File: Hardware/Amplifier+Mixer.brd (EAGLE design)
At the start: 140 x 140 mm, 192 parts, among them IC1 7812, IC2 7805, IC3 7912, IC4 OPA134PA, IC5 OPA134PA, IC6 MEGA8-AI, IC7 74HCT04, IC8 LM358D, IC9 LM358D, J1 6MM, J10 JST-XH2, J2 6MM, J3 6MM, J4 6MM, J5 TERMINAL-BLOCK-2PLUG-IN, J6 TERMINAL-BLOCK-2PLUG-IN, J7 ENCODER, J8 DISPLAY, J9 USB, K1 12V 8A, K2 12V 8A, T1 BC817, T2 BC817, T3 BC817, T4 BC817, U1 LM1117-3.3, U2 10k, U3 10k, U4 10k, U5 10k, U6 TDA7498L, U7 10k, U8 10k, X1 RCA-4-CHANNEL, X2 JST-XH2, X3 ICSP

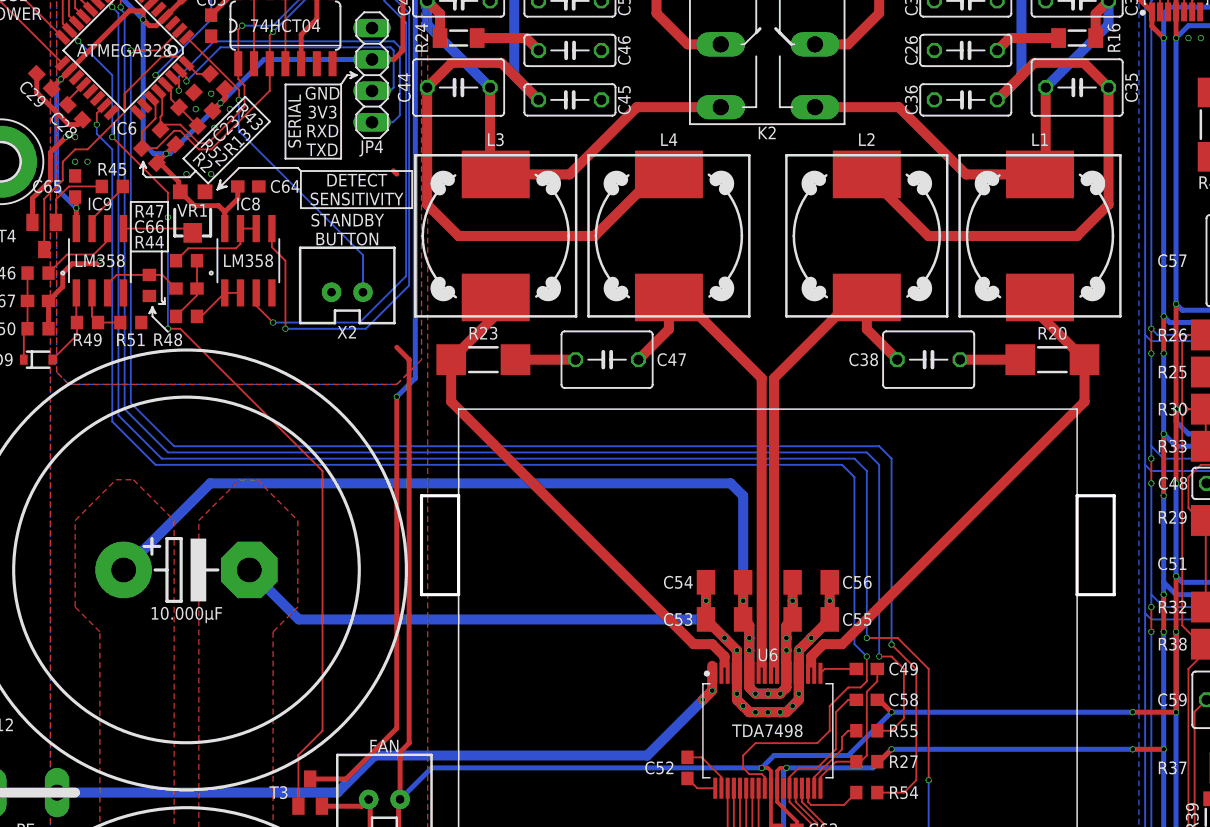
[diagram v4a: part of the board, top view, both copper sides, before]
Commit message: added temp sensor for amp chip heatsink
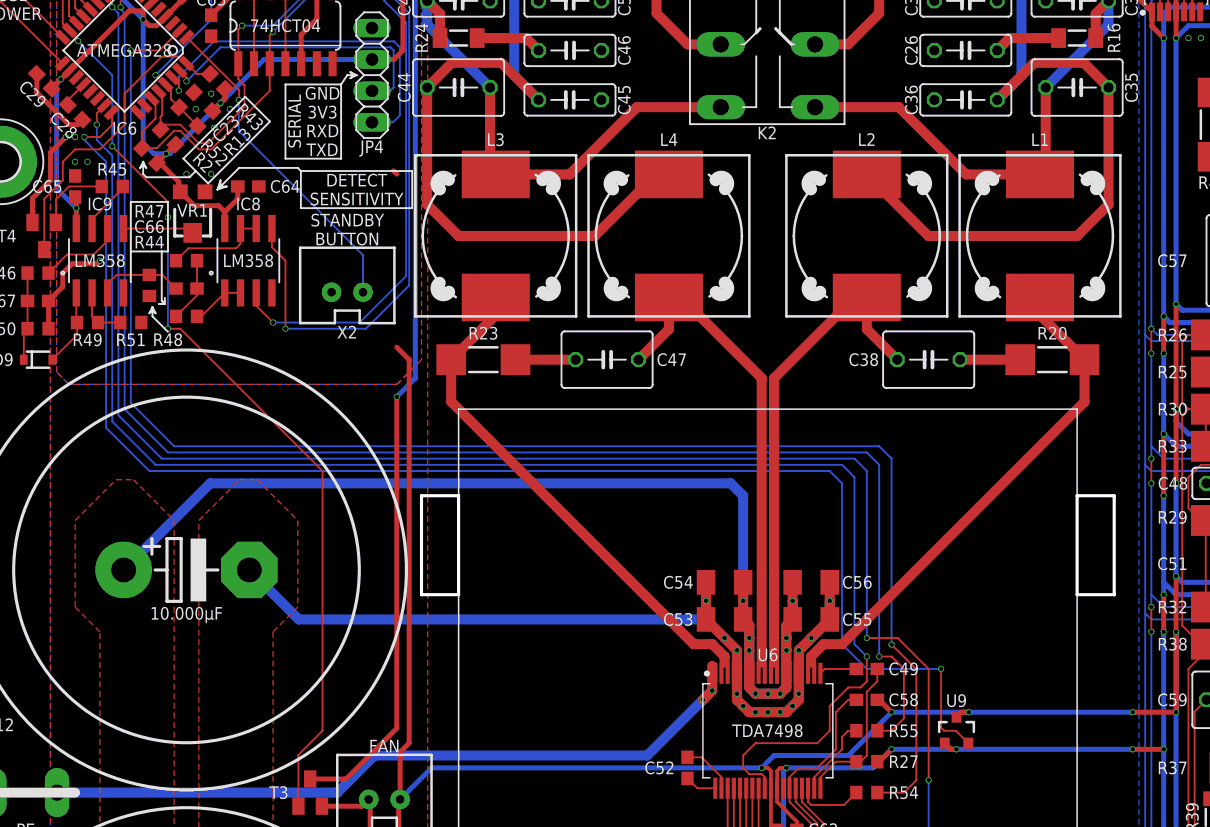
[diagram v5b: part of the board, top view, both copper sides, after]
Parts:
- added U9: MCP9700SMD, SparkFun-Sensors:SOT23-3
- renumbered U$1 to KK3
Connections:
- new net T_SENSE: IC6.24, U9.2
- net +3V3: now also U9.1
- net DGND: now also U9.3
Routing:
- net T_SENSE: track 0.00 -> 118.6 mm, vias 0 -> 2
- net DGND: track 407.7 -> 408.8 mm, vias 36 -> 37
- net +3V3: track 492.7 -> 493.8 mm, vias 26 -> 27
- net AUDIO_DETECT: track 24.6 -> 25.2 mm
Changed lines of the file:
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@@
 <attribute name="STOCK" value="0" x="5" y="127" size="1.778" layer="27" rot="R270" display="off"/>
 </element>
-<element name="U$1" library="Class D Amp" library_urn="urn:adsk.eagle:library:8719353" package="HEATSINK-PENTIUM" package3d_urn="urn:adsk.eagle:package:8803895/4" value="HEATSINK-PENTIUM" x="66" y="60" smashed="yes">
+<element name="KK3" library="Class D Amp" library_urn="urn:adsk.eagle:library:8719353" package="HEATSINK-PENTIUM" package3d_urn="urn:adsk.eagle:package:8803895/4" value="HEATSINK-PENTIUM" x="66" y="60" smashed="yes">
 <attribute name="STOCK" value="1" x="66" y="60" size="1.778" layer="27" display="off"/>
 </element>
@@
 <attribute name="VALUE" x="131.5" y="6.893" size="0.6096" layer="28" font="vector" ratio="20" rot="MR180" align="top-center"/>
 </element>
+<element name="U9" library="SparkFun-Sensors" package="SOT23-3" value="MCP9700SMD" x="81.25" y="60" smashed="yes">
+<attribute name="NAME" x="81.25" y="61.927" size="1.016" layer="25" align="bottom-center"/>
+<attribute name="PROD_ID" value="IC-08917" x="81.25" y="60" size="1.016" layer="27" ratio="14" display="off"/>
+<attribute name="VALUE" x="80.234" y="59.8095" size="0.4064" layer="27"/>
+</element>
 </elements>
 <signals>
@@
 <wire x1="75" y1="57.5" x2="76" y2="58.5" width="0.4064" layer="1"/>
 <via x="76" y="58.5" extent="1-16" drill="0.35" shape="octagon"/>
-<wire x1="95.5" y1="58.5" x2="76" y2="58.5" width="0.4064" layer="16"/>
+<wire x1="95.5" y1="58.5" x2="81.25" y2="58.5" width="0.4064" layer="16"/>
 <via x="95.5" y="58.5" extent="1-16" drill="0.35" shape="octagon"/>
+<wire x1="81.25" y1="58.5" x2="76" y2="58.5" width="0.4064" layer="16"/>
 <wire x1="98" y1="58.5" x2="95.5" y2="58.5" width="0.4064" layer="1"/>
 <via x="98" y="58.5" extent="1-16" drill="0.35" shape="octagon"/>
@@
 <wire x1="18.374996875" y1="104.375" x2="18.374996875" y2="103.700003125" width="0.4064" layer="1"/>
 <wire x1="18.374996875" y1="103.700003125" x2="18.5" y2="103.575" width="0.4064" layer="1"/>
+<contactref element="U9" pad="1"/>
+<wire x1="80.3" y1="59" x2="80.8" y2="58.5" width="0.4064" layer="1"/>
+<wire x1="80.8" y1="58.5" x2="81.25" y2="58.5" width="0.4064" layer="1"/>
+<via x="81.25" y="58.5" extent="1-16" drill="0.35" shape="octagon"/>
 </signal>
 <signal name="N$37">
@@
 <wire x1="18.459796875" y1="114.5" x2="17" y2="114.5" width="0.1524" layer="1"/>
 <wire x1="17" y1="114.5" x2="14" y2="111.5" width="0.1524" layer="1"/>
-<wire x1="14" y1="111.5" x2="14" y2="110" width="0.1524" layer="1"/>
-<wire x1="14" y1="110" x2="11" y2="107" width="0.1524" layer="1"/>
-<wire x1="11" y1="107" x2="10" y2="107" width="0.1524" layer="1"/>
+<wire x1="14" y1="111.5" x2="14" y2="109" width="0.1524" layer="1"/>
+<wire x1="14" y1="109" x2="12" y2="107" width="0.1524" layer="1"/>
+<wire x1="12" y1="107" x2="10" y2="107" width="0.1524" layer="1"/>
 <wire x1="20.89895625" y1="113.101040625" x2="19.85875625" y2="113.101040625" width="0.1524" layer="1"/>
 <wire x1="19.85875625" y1="113.101040625" x2="19.015225" y2="113.944571875" width="0.1524" layer="1"/>
@@
 <wire x1="71" y1="62" x2="72.5" y2="63.5" width="0.1524" layer="1"/>
 <wire x1="16.5" y1="81.5" x2="13" y2="85" width="0.1524" layer="16"/>
-<wire x1="11.75" y1="108.25" x2="11.75" y2="109" width="0.1524" layer="16"/>
+<wire x1="11.75" y1="107.75" x2="11.75" y2="109" width="0.1524" layer="16"/>
 <via x="11.75" y="109" extent="1-16" drill="0.35" shape="octagon"/>
 <wire x1="72" y1="81.5" x2="16.5" y2="81.5" width="0.1524" layer="16"/>
-<wire x1="13" y1="85" x2="13" y2="107" width="0.1524" layer="16"/>
-<wire x1="13" y1="107" x2="11.75" y2="108.25" width="0.1524" layer="16"/>
+<wire x1="13" y1="85" x2="13" y2="106.5" width="0.1524" layer="16"/>
+<wire x1="13" y1="106.5" x2="11.75" y2="107.75" width="0.1524" layer="16"/>
 </signal>
 <signal name="AMP_MUTE">
@@
 <wire x1="75" y1="62.5" x2="76" y2="61.5" width="0.4064" layer="1"/>
 <via x="76" y="61.5" extent="1-16" drill="0.35" shape="octagon"/>
-<wire x1="95.5" y1="61.5" x2="76" y2="61.5" width="0.4064" layer="16"/>
+<wire x1="95.5" y1="61.5" x2="82.25" y2="61.5" width="0.4064" layer="16"/>
 <via x="95.5" y="61.5" extent="1-16" drill="0.35" shape="octagon"/>
+<wire x1="82.25" y1="61.5" x2="76" y2="61.5" width="0.4064" layer="16"/>
 <wire x1="99" y1="61.5" x2="95.5" y2="61.5" width="0.4064" layer="1"/>
 <via x="99" y="61.5" extent="1-16" drill="0.35" shape="octagon"/>
@@
 <wire x1="130.575" y1="34.575" x2="130.575" y2="33.155" width="0.4064" layer="16"/>
 <via x="130.075" y="35.075" extent="1-16" drill="0.35" shape="octagon"/>
+<contactref element="U9" pad="3"/>
+<wire x1="82.25" y1="61.5" x2="81.65" y2="61.5" width="0.4064" layer="1"/>
+<wire x1="81.25" y1="61.1" x2="81.65" y2="61.5" width="0.4064" layer="1"/>
+<via x="82.25" y="61.5" extent="1-16" drill="0.35" shape="octagon"/>
 </signal>
 <signal name="AGND">
@@
 <wire x1="9" y1="117.171571875" x2="9.550459375" y2="116.6211125" width="0.1524" layer="1"/>
 <wire x1="9" y1="124" x2="9" y2="117.171571875" width="0.1524" layer="1"/>
-<wire x1="13" y1="108" x2="17.5" y2="103.5" width="0.1524" layer="1"/>
+<wire x1="17.5" y1="102.75" x2="13" y2="107.25" width="0.1524" layer="1"/>
 <via x="17.5" y="101.5" extent="1-16" drill="0.35" shape="octagon"/>
 <wire x1="17.5" y1="101.5" x2="17.5" y2="92.5" width="0.1524" layer="16"/>
@@
 <wire x1="28" y1="58" x2="28.05" y2="57.95" width="0.1524" layer="1"/>
 <wire x1="28.05" y1="57.95" x2="28.05" y2="53.9" width="0.1524" layer="1"/>
-<wire x1="17.5" y1="103.5" x2="17.5" y2="101.5" width="0.1524" layer="1"/>
+<wire x1="17.5" y1="102.75" x2="17.5" y2="101.5" width="0.1524" layer="1"/>
 <wire x1="9.550459375" y1="116.6211125" x2="10.25" y2="115.921571875" width="0.1524" layer="1"/>
 <wire x1="10.25" y1="115.921571875" x2="10.25" y2="115.75" width="0.1524" layer="1"/>
 <via x="10.25" y="115.75" extent="1-16" drill="0.35" shape="octagon"/>
-<wire x1="13" y1="113" x2="13" y2="108" width="0.1524" layer="16"/>
+<wire x1="13" y1="113" x2="13" y2="107.25" width="0.1524" layer="16"/>
 <wire x1="13" y1="113" x2="10.25" y2="115.75" width="0.1524" layer="16"/>
-<via x="13" y="108" extent="1-16" drill="0.35" shape="octagon"/>
+<via x="13" y="107.25" extent="1-16" drill="0.35" shape="octagon"/>
 </signal>
 <signal name="N$45">
@@
 <wire x1="98.02" y1="37.54" x2="98" y2="37.56" width="0.1524" layer="1"/>
 </signal>
+<signal name="T_SENSE">
+<contactref element="U9" pad="2"/>
+<contactref element="IC6" pad="24"/>
+<wire x1="82.2" y1="59" x2="81.2" y2="60" width="0.1524" layer="1"/>
+<wire x1="81.2" y1="60" x2="80.25" y2="60" width="0.1524" layer="1"/>
+<wire x1="80.25" y1="60" x2="80" y2="60.25" width="0.1524" layer="1"/>
+<wire x1="80" y1="60.25" x2="80" y2="65" width="0.1524" layer="1"/>
+<via x="80" y="65" extent="1-16" drill="0.35" shape="octagon"/>
+<wire x1="80" y1="65" x2="74" y2="65" width="0.1524" layer="16"/>
+<wire x1="74" y1="65" x2="72" y2="67" width="0.1524" layer="16"/>
+<wire x1="72" y1="67" x2="72" y2="80" width="0.1524" layer="16"/>
+<wire x1="72" y1="80" x2="71" y2="81" width="0.1524" layer="16"/>
+<wire x1="71" y1="81" x2="16" y2="81" width="0.1524" layer="16"/>
+<wire x1="16" y1="81" x2="12.5" y2="84.5" width="0.1524" layer="16"/>
+<wire x1="12.5" y1="84.5" x2="12.5" y2="106" width="0.1524" layer="16"/>
+<wire x1="10.75" y1="107.75" x2="10.75" y2="108" width="0.1524" layer="16"/>
+<via x="10.75" y="108" extent="1-16" drill="0.35" shape="octagon"/>
+<wire x1="12" y1="108" x2="10.75" y2="108" width="0.1524" layer="1"/>
+<wire x1="12.5" y1="106" x2="10.75" y2="107.75" width="0.1524" layer="16"/>
+<wire x1="12.944571875" y1="109.984771875" x2="13" y2="109.92934375" width="0.1524" layer="1"/>
+<wire x1="13" y1="109.92934375" x2="13" y2="109" width="0.1524" layer="1"/>
+<wire x1="13" y1="109" x2="12" y2="108" width="0.1524" layer="1"/>
+</signal>
 </signals>

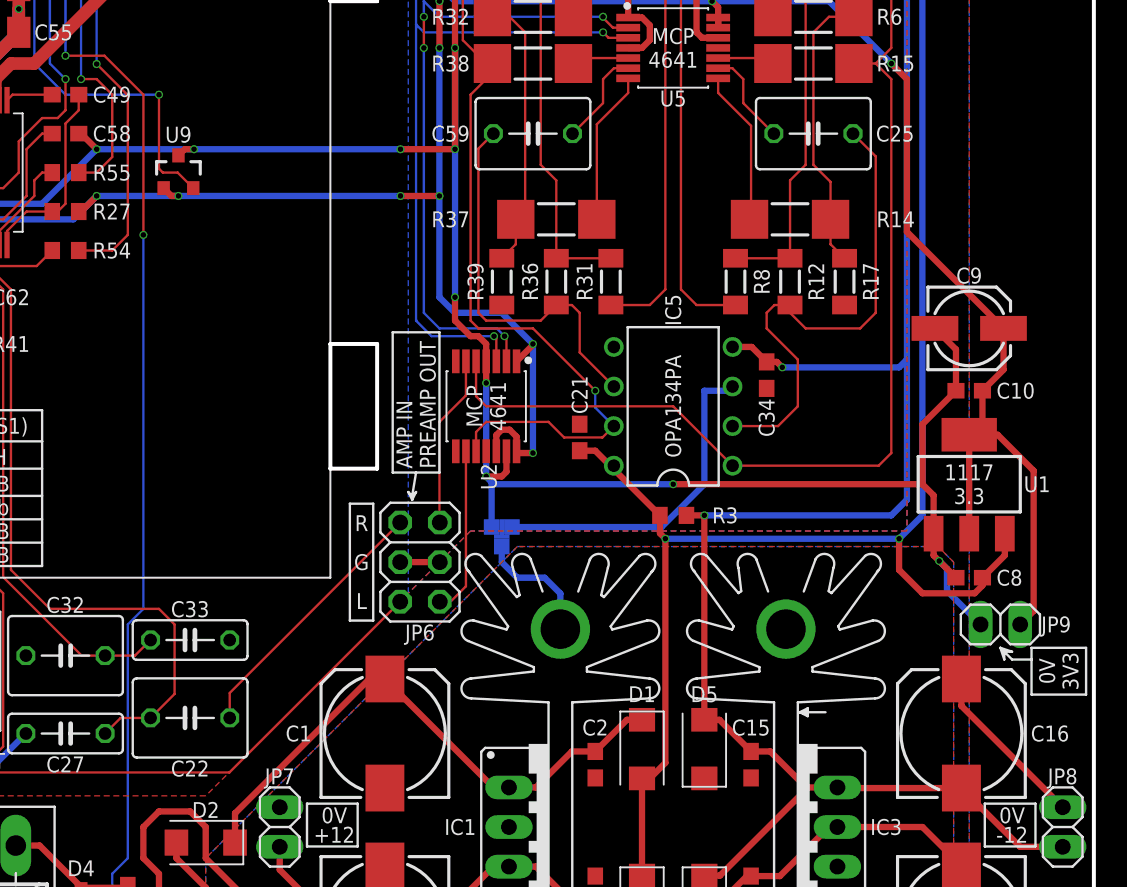
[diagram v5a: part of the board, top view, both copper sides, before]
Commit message: improved temp sensor routing
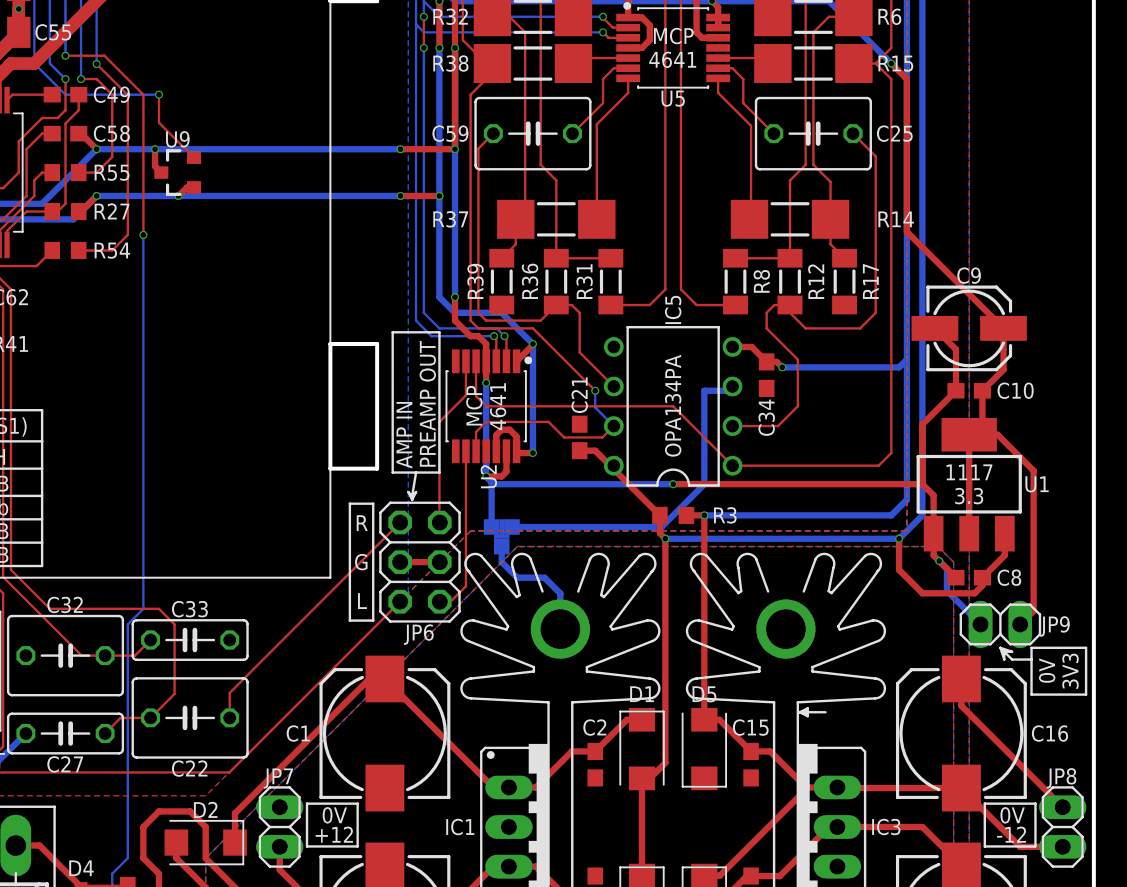
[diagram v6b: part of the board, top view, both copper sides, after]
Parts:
- turned U9 to 90 degrees
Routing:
- net T_SENSE: track 118.6 -> 116.1 mm
- net DGND: track 408.8 -> 409.3 mm
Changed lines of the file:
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@@
 </element>
 <element name="JP7" library="pinhead" library_urn="urn:adsk.eagle:library:325" package="1X02" package3d_urn="urn:adsk.eagle:package:22435/2" value="" x="87.75" y="18" smashed="yes" rot="R270">
-<attribute name="NAME" x="87.75" y="20.7432" size="1.016" layer="25" ratio="10" align="bottom-center"/>
+<attribute name="NAME" x="87.75" y="20.7432" size="1.016" layer="25" ratio="14" align="bottom-center"/>
 <attribute name="VALUE" x="84.575" y="20.54" size="1.27" layer="27" rot="R270"/>
 </element>
 <element name="JP8" library="pinhead" library_urn="urn:adsk.eagle:library:325" package="1X02" package3d_urn="urn:adsk.eagle:package:22435/2" value="" x="138" y="18" smashed="yes" rot="R270">
-<attribute name="NAME" x="138" y="20.7432" size="1.016" layer="25" ratio="10" align="bottom-center"/>
+<attribute name="NAME" x="138" y="20.7432" size="1.016" layer="25" ratio="14" align="bottom-center"/>
 <attribute name="VALUE" x="134.825" y="20.54" size="1.27" layer="27" rot="R270"/>
 </element>
 <element name="JP9" library="pinhead" library_urn="urn:adsk.eagle:library:325" package="1X02" package3d_urn="urn:adsk.eagle:package:22435/2" value="" x="134" y="31" smashed="yes">
-<attribute name="NAME" x="136.6162" y="31" size="1.016" layer="25" ratio="10" align="center-left"/>
+<attribute name="NAME" x="136.6162" y="31" size="1.016" layer="25" ratio="14" align="center-left"/>
 <attribute name="VALUE" x="131.46" y="27.825" size="1.27" layer="27"/>
 </element>
 <element name="JP10" library="SparkFun-Jumpers" library_urn="urn:adsk.eagle:library:528" package="SMT-JUMPER_2_NO_NO-SILK" package3d_urn="urn:adsk.eagle:package:39277/1" value="PEGND" x="131.5" y="5.75" smashed="yes" rot="MR180">
-<attribute name="NAME" x="130.75" y="4.857" size="1.016" layer="26" ratio="20" rot="MR180" align="bottom-center"/>
+<attribute name="NAME" x="130.75" y="4.857" size="1.016" layer="26" ratio="14" rot="MR180" align="bottom-center"/>
 <attribute name="VALUE" x="131.5" y="6.893" size="0.6096" layer="28" font="vector" ratio="20" rot="MR180" align="top-center"/>
 </element>
-<element name="U9" library="SparkFun-Sensors" package="SOT23-3" value="MCP9700SMD" x="81.25" y="60" smashed="yes">
-<attribute name="NAME" x="81.25" y="61.927" size="1.016" layer="25" align="bottom-center"/>
-<attribute name="PROD_ID" value="IC-08917" x="81.25" y="60" size="1.016" layer="27" ratio="14" display="off"/>
-<attribute name="VALUE" x="80.234" y="59.8095" size="0.4064" layer="27"/>
+<element name="U9" library="SparkFun-Sensors" package="SOT23-3" value="MCP9700SMD" x="81.25" y="60" smashed="yes" rot="R90">
+<attribute name="NAME" x="81.2" y="61.6286" size="1.016" layer="25" ratio="14" align="bottom-center"/>
+<attribute name="PROD_ID" value="IC-08917" x="81.25" y="60" size="1.016" layer="27" ratio="14" rot="R90" display="off"/>
+<attribute name="VALUE" x="81.4405" y="58.984" size="0.4064" layer="27" rot="R90"/>
 </element>
 </elements>
@@
 <wire x1="18.374996875" y1="103.700003125" x2="18.5" y2="103.575" width="0.4064" layer="1"/>
 <contactref element="U9" pad="1"/>
-<wire x1="80.3" y1="59" x2="80.8" y2="58.5" width="0.4064" layer="1"/>
-<wire x1="80.8" y1="58.5" x2="81.25" y2="58.5" width="0.4064" layer="1"/>
 <via x="81.25" y="58.5" extent="1-16" drill="0.35" shape="octagon"/>
+<wire x1="81.25" y1="58.5" x2="81.8" y2="59.05" width="0.4064" layer="1"/>
+<wire x1="81.8" y1="59.05" x2="82.25" y2="59.05" width="0.4064" layer="1"/>
 </signal>
 <signal name="N$37">
@@
 <wire x1="75" y1="62.5" x2="76" y2="61.5" width="0.4064" layer="1"/>
 <via x="76" y="61.5" extent="1-16" drill="0.35" shape="octagon"/>
-<wire x1="95.5" y1="61.5" x2="82.25" y2="61.5" width="0.4064" layer="16"/>
+<wire x1="95.5" y1="61.5" x2="79.75" y2="61.5" width="0.4064" layer="16"/>
 <via x="95.5" y="61.5" extent="1-16" drill="0.35" shape="octagon"/>
-<wire x1="82.25" y1="61.5" x2="76" y2="61.5" width="0.4064" layer="16"/>
+<wire x1="79.75" y1="61.5" x2="76" y2="61.5" width="0.4064" layer="16"/>
 <wire x1="99" y1="61.5" x2="95.5" y2="61.5" width="0.4064" layer="1"/>
 <via x="99" y="61.5" extent="1-16" drill="0.35" shape="octagon"/>
@@
 <via x="130.075" y="35.075" extent="1-16" drill="0.35" shape="octagon"/>
 <contactref element="U9" pad="3"/>
-<wire x1="82.25" y1="61.5" x2="81.65" y2="61.5" width="0.4064" layer="1"/>
-<wire x1="81.25" y1="61.1" x2="81.65" y2="61.5" width="0.4064" layer="1"/>
-<via x="82.25" y="61.5" extent="1-16" drill="0.35" shape="octagon"/>
+<wire x1="79.75" y1="61.5" x2="79.75" y2="60.4" width="0.4064" layer="1"/>
+<wire x1="80.15" y1="60" x2="79.75" y2="60.4" width="0.4064" layer="1"/>
+<via x="79.75" y="61.5" extent="1-16" drill="0.35" shape="octagon"/>
 </signal>
 <signal name="AGND">
@@
 <contactref element="U9" pad="2"/>
 <contactref element="IC6" pad="24"/>
-<wire x1="82.2" y1="59" x2="81.2" y2="60" width="0.1524" layer="1"/>
-<wire x1="81.2" y1="60" x2="80.25" y2="60" width="0.1524" layer="1"/>
-<wire x1="80.25" y1="60" x2="80" y2="60.25" width="0.1524" layer="1"/>
-<wire x1="80" y1="60.25" x2="80" y2="65" width="0.1524" layer="1"/>
 <via x="80" y="65" extent="1-16" drill="0.35" shape="octagon"/>
 <wire x1="80" y1="65" x2="74" y2="65" width="0.1524" layer="16"/>
@@
 <wire x1="13" y1="109.92934375" x2="13" y2="109" width="0.1524" layer="1"/>
 <wire x1="13" y1="109" x2="12" y2="108" width="0.1524" layer="1"/>
+<wire x1="80" y1="63.2" x2="80" y2="65" width="0.1524" layer="1"/>
+<wire x1="82.25" y1="60.95" x2="80" y2="63.2" width="0.1524" layer="1"/>
 </signal>
 </signals>
